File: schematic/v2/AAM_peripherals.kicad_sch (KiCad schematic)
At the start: 29 parts, among them J12 AAM_DBG, J19 AudioJack3, J21 USB_A, J23 USB_A, J3 LCD_display, U32 CH340G, Y1 Crystal

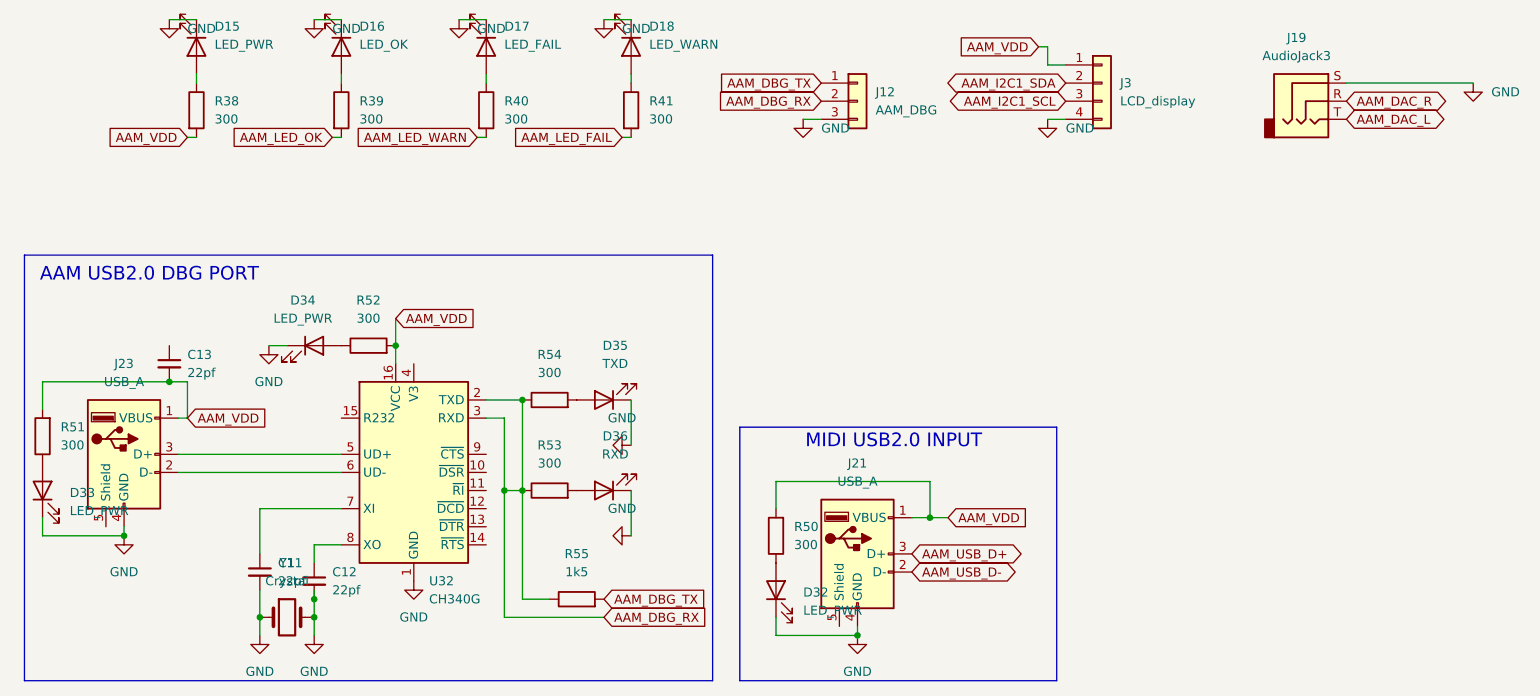
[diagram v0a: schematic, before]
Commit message: adding more sheets in the schematic
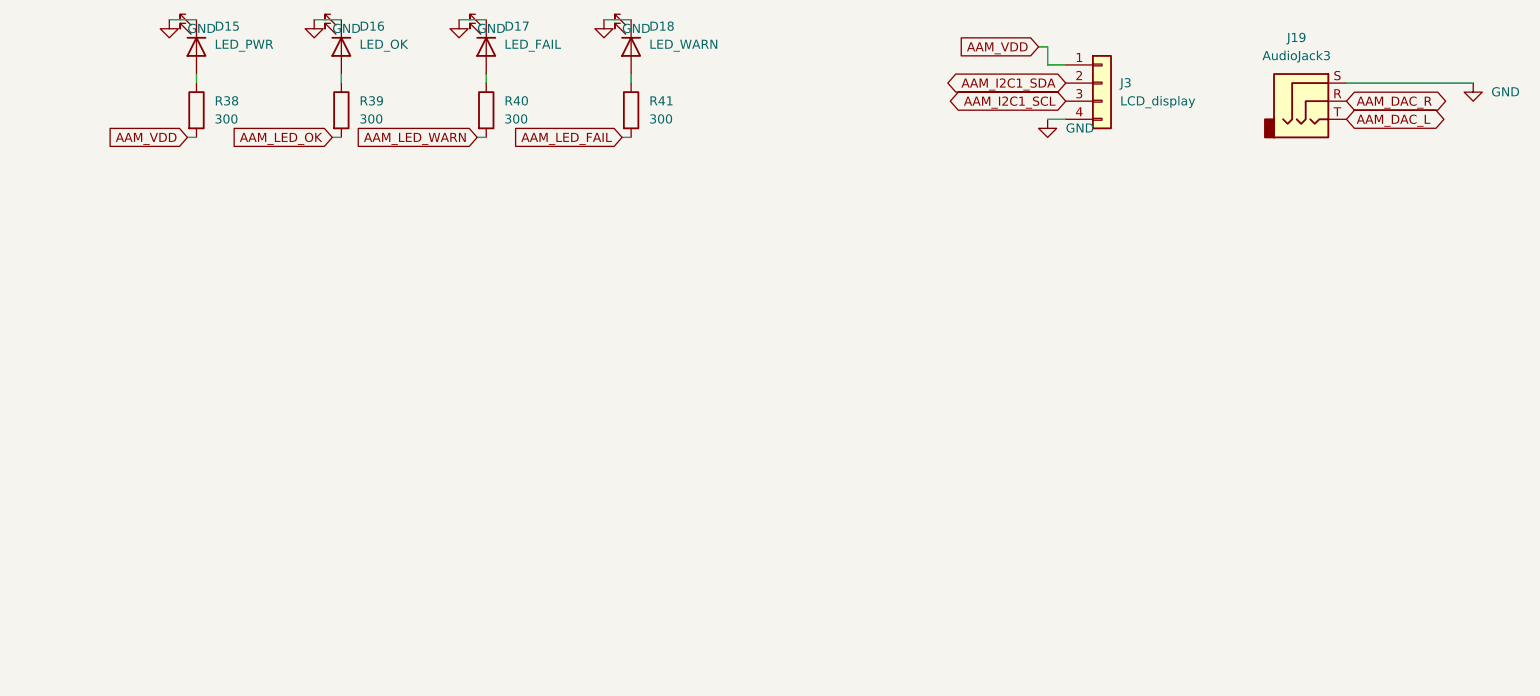
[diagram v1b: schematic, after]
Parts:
- removed C11, C12, C13: 22pf, Capacitor_SMD:C_0805_2012Metric, symbol Device:C_Small
- removed D32, D33, D34: LED_PWR, LED_SMD:LED_0603_1608Metric, symbol Device:LED
- removed D35: TXD, LED_SMD:LED_0603_1608Metric, symbol Device:LED
- removed D36: RXD, LED_SMD:LED_0603_1608Metric, symbol Device:LED
- removed J12: AAM_DBG, Connector_PinHeader_1.00mm:PinHeader_1x03_P1.00mm_Horizontal, symbol Connector_Generic:Conn_01x03
- removed J21, J23: USB_A, Connector_USB:USB_A_CNCTech_1001-011-01101_Horizontal, symbol Connector:USB_A
- removed R50, R51, R52, R53, R54: 300, Resistor_SMD:R_0805_2012Metric_Pad1.20x1.40mm_HandSolder, symbol Device:R
- removed R55: 1k5, Resistor_SMD:R_0805_2012Metric_Pad1.20x1.40mm_HandSolder, symbol Device:R
- removed U32: CH340G, Package_SO:SOIC-16_3.9x9.9mm_P1.27mm, symbol Interface_USB:CH340G
- removed Y1: Crystal, symbol Device:Crystal
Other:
- note removed: "AAM USB2.0 DBG PORT"
- note removed: "MIDI USB2.0 INPUT"
